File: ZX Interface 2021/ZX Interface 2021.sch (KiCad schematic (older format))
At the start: 50 parts, among them J1 AJS #1, J2 AJS #2, J3 SWAP_ROMS, J4 Cartridge, J5 JOYSTICK_EN, M1 Mounting, M2 Mounting, M3 Mounting, M4 Mounting, M5 Mounting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

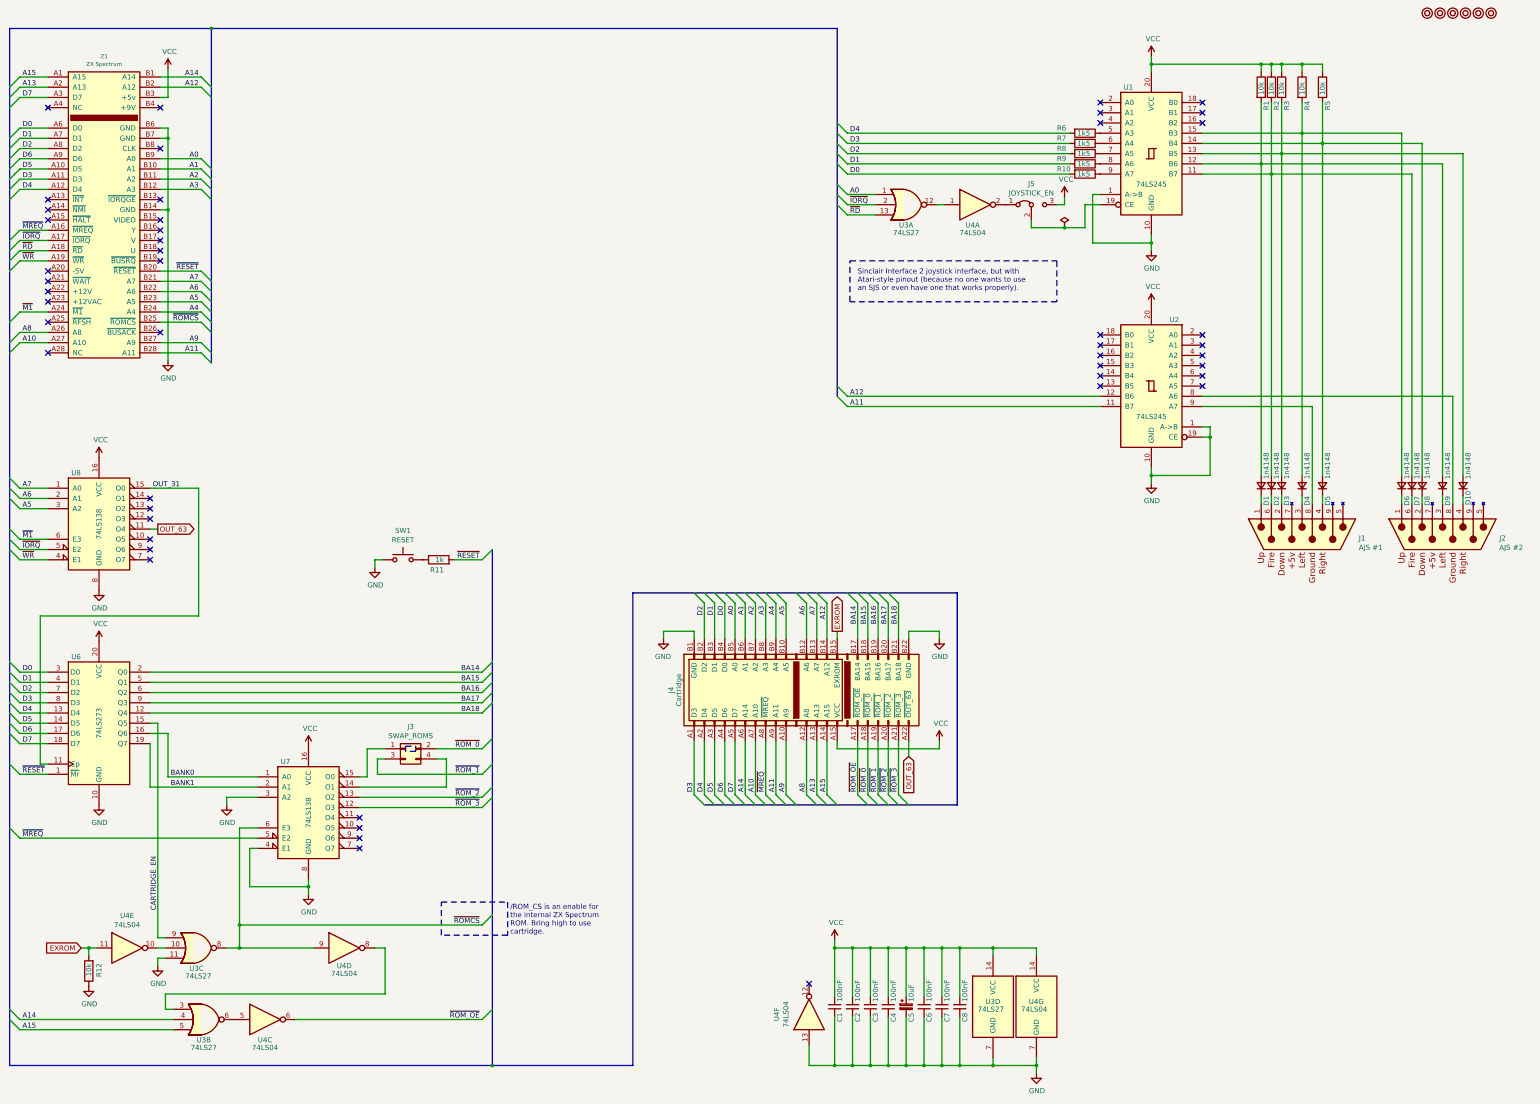
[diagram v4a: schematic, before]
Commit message: Added some artwork
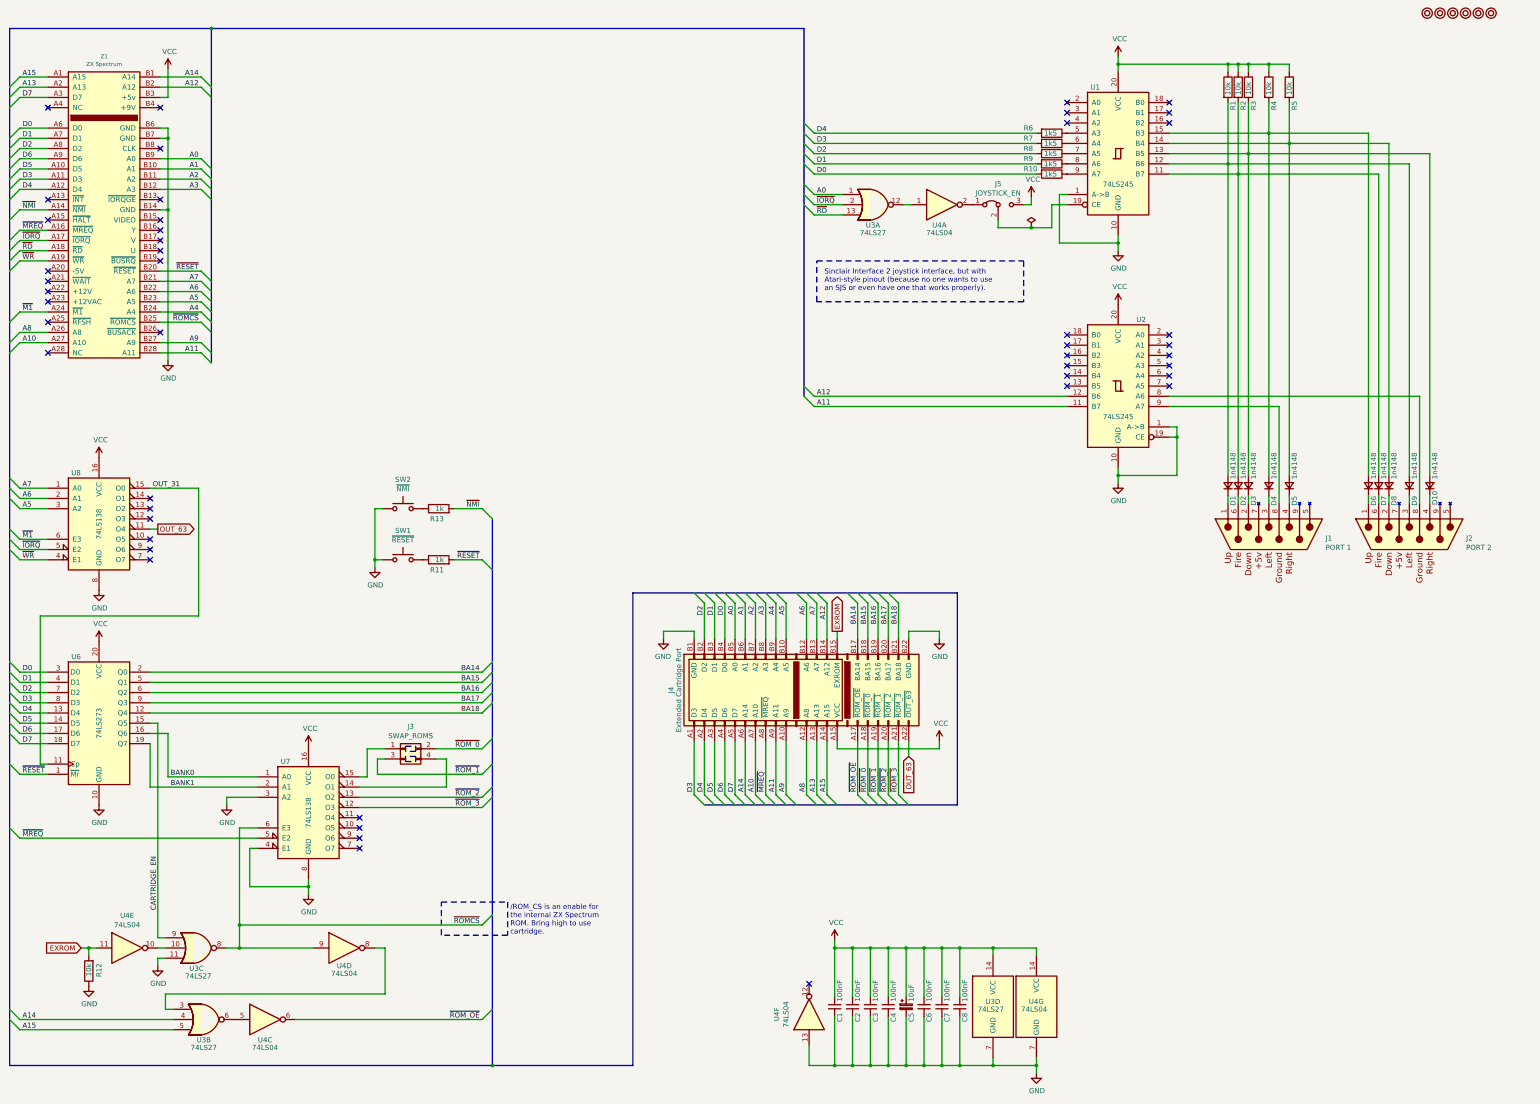
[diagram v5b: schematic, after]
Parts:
- added R13: 1k, Resistor_THT:R_Axial_DIN0207_L6.3mm_D2.5mm_P10.16mm_Horizontal, symbol Device:R
- added SW2: ~NMI, switch_cutout:SW_PUSH_6mm, symbol Switch:SW_Push
- J1: value AJS #1 -> PORT 1
- J2: value AJS #2 -> PORT 2
- J4: value Cartridge -> Extended Cartridge Port
- SW1: value RESET -> ~RESET
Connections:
- net GND: now also SW2.1
- net ~NMI: now reaches Z1.A14 (~NMI)
- net ~NMI: now also R13.2
- new net: R13.1, SW2.2
- no-connect marks 48 -> 47
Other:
- moved on the sheet: D1, D10, D2, D3, D4, D5, D6, D7, D8, D9, J1, J2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

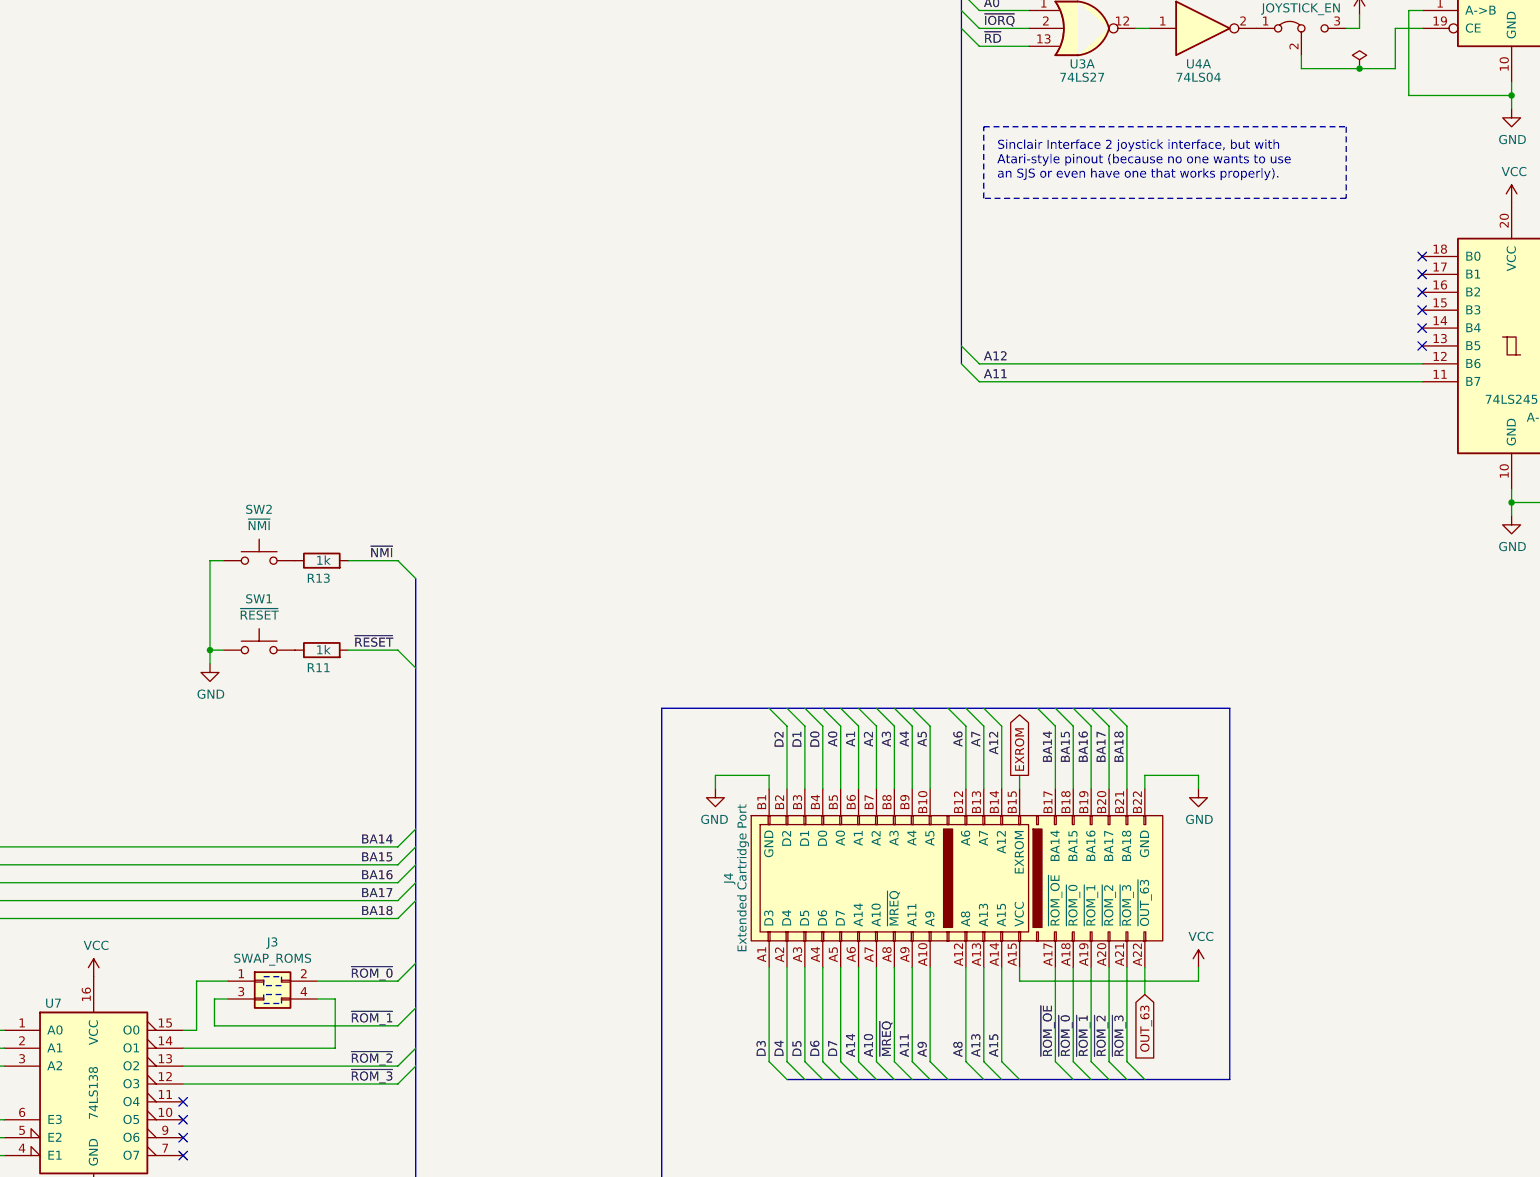
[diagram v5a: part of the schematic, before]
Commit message: Cartridge pins were mirrored, still need to change cartridges
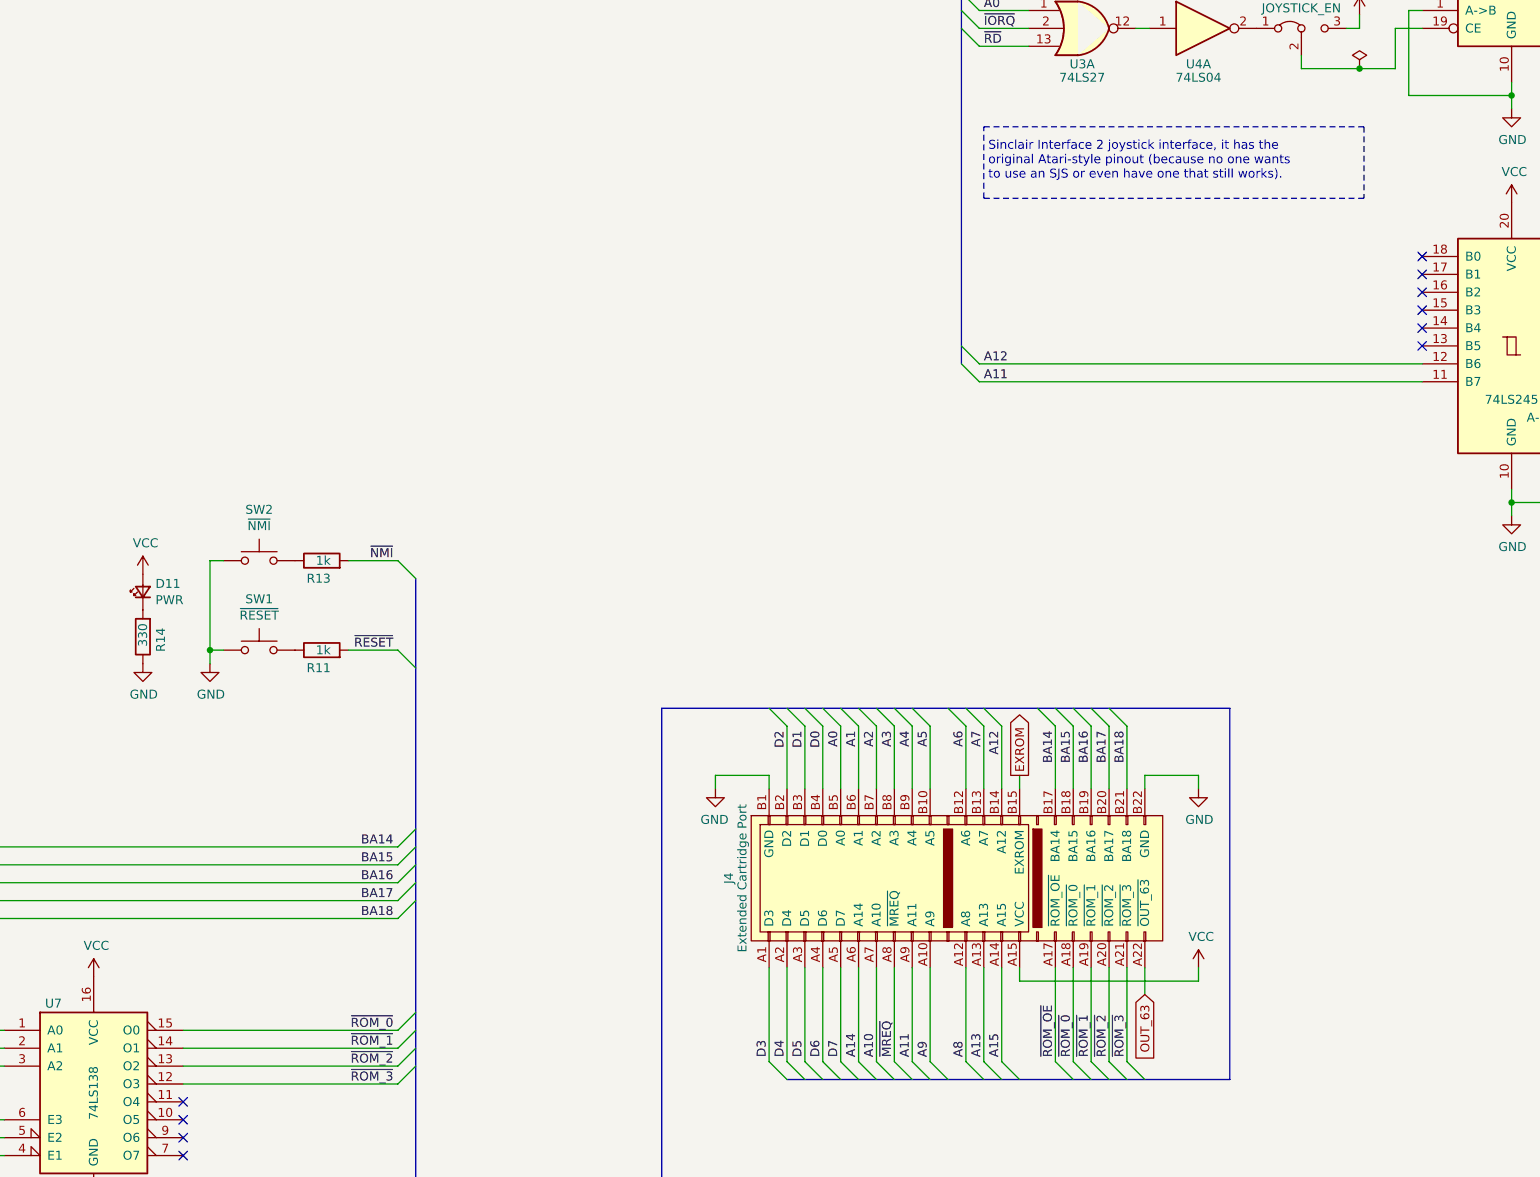
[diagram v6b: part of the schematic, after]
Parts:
- removed J3: SWAP_ROMS, Connector_PinHeader_2.54mm:PinHeader_2x02_P2.54mm_Vertical, symbol Connector_Generic:Conn_02x02_Odd_Even
- added D11: PWR, LED_THT:LED_D5.0mm, symbol Device:LED_Small
- added R14: 330, Resistor_THT:R_Axial_DIN0207_L6.3mm_D2.5mm_P10.16mm_Horizontal, symbol Device:R
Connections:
- net GND: now also R14.1
- net VCC: now also D11.2 (A)
- net ~ROM_0: now also U7.15 (O0)
- net ~ROM_1: now also U7.14 (O1)
- new net: D11.1 (K), R14.2
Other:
- note added: "Sinclair Interface 2 joystick interface, it has the \noriginal Atari-style pinout (because no one wants\nto use an SJS or even have one that still works)."
- note removed: "Sinclair Interface 2 joystick interface, but with\nAtari-style pinout (because no one wants to use\nan SJS or even have one that works properly)."
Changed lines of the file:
@@
 NoConn ~ 4900 8725
 Entry Wire Line
-	6100 8000 6200 7900
+	6100 8125 6200 8025
 NoConn ~ 9300 10050
 NoConn ~ 1850 3575
-$Comp
-L Connector_Generic:Conn_02x02_Odd_Even J3
-U 1 1 61A0CB30
-P 5350 7750
-F 0 "J3" H 5400 7967 50  0000 C CNN
-F 1 "SWAP_ROMS" H 5400 7876 50  0000 C CNN
-F 2 "Connector_PinHeader_2.54mm:PinHeader_2x02_P2.54mm_Vertical" H 5350 7750 50  0001 C CNN
-F 3 "~" H 5350 7750 50  0001 C CNN
-	1    5350 7750
-	1    0    0    -1
-$EndComp
-Entry Wire Line
-	6100 7750 6200 7650
+Entry Wire Line
+	6100 8025 6200 7925
 Entry Wire Line
 	6100 8325 6200 8225
 Entry Wire Line
 	6100 8225 6200 8125
-Text Label 6075 8000 2    50   ~ 0
+Text Label 6075 8125 2    50   ~ 0
 ~ROM_1
-Text Label 6075 7750 2    50   ~ 0
+Text Label 6075 8025 2    50   ~ 0
 ~ROM_0
 Entry Wire Line
@@
 	2850 7400 6100 7400
 Wire Wire Line
-	6100 7750 5650 7750
-Wire Notes Line
-	5450 7775 5350 7775
-Wire Notes Line
-	5450 7725 5450 7775
-Wire Notes Line
-	5350 7725 5450 7725
-Wire Notes Line
-	5350 7775 5350 7725
-Wire Wire Line
-	5750 7850 5750 8125
-Wire Wire Line
-	5650 7850 5750 7850
-Wire Wire Line
-	5075 8000 6100 8000
-Wire Wire Line
-	5075 7850 5150 7850
-Wire Wire Line
-	5075 8000 5075 7850
-Wire Wire Line
-	4975 7750 5150 7750
-Wire Wire Line
-	4975 8025 4975 7750
-Wire Wire Line
 	9300 10650 9300 10850
 Wire Wire Line
@@
 Wire Wire Line
 	2850 8125 3900 8125
-Wire Wire Line
-	4900 8025 4975 8025
-Wire Wire Line
-	4900 8125 5750 8125
 Wire Wire Line
 	4900 8225 6100 8225
@@
 Text Notes 6375 9575 0    50   ~ 0
 /ROM_CS is an enable for\nthe internal ZX Spectrum\nROM. Bring high to use\ncartridge.
-Text Notes 9450 3275 0    50   ~ 0
-Sinclair Interface 2 joystick interface, but with\nAtari-style pinout (because no one wants to use\nan SJS or even have one that works properly).
+Text Notes 9400 3275 0    50   ~ 0
+Sinclair Interface 2 joystick interface, it has the \noriginal Atari-style pinout (because no one wants\nto use an SJS or even have one that still works).
 Wire Notes Line
-	9375 2975 11400 2975
-Wire Notes Line
-	11400 2975 11400 3375
-Wire Notes Line
-	11400 3375 9375 3375
+	11500 2975 11500 3375
 Wire Notes Line
 	9375 3375 9375 2975
@@
 	11150 2650 11150 2575
 Wire Wire Line
-	11150 2650 11475 2650
-Connection ~ 11475 2650
-Wire Wire Line
-	11475 2650 11675 2650
-Wire Wire Line
 	11675 2650 11675 2425
 Wire Wire Line
 	11675 2425 11825 2425
-$Comp
-L power:PWR_FLAG #FLG0101
-U 1 1 607D1200
-P 11475 2650
-F 0 "#FLG0101" H 11475 2725 50  0001 C CNN
-F 1 "PWR_FLAG" H 11475 2823 50  0001 C CNN
-F 2 "" H 11475 2650 50  0001 C CNN
-F 3 "~" H 11475 2650 50  0001 C CNN
-	1    11475 2650
-	1    0    0    -1
-$EndComp
 Wire Bus Line
 	9250 700  3450 700
@@
 Text Label 1600 2475 0    50   ~ 0
 ~NMI
+$Comp
+L Device:R R14
+U 1 1 60553925
+P 4675 5825
+F 0 "R14" V 4575 5775 50  0000 L CNN
+F 1 "330" V 4675 5750 50  0000 L CNN
+F 2 "Resistor_THT:R_Axial_DIN0207_L6.3mm_D2.5mm_P10.16mm_Horizontal" V 4605 5825 50  0001 C CNN
+F 3 "~" H 4675 5825 50  0001 C CNN
+	1    4675 5825
+	-1   0    0    1
+$EndComp
+$Comp
+L Device:LED_Small D11
+U 1 1 6059C36A
+P 4675 5575
+F 0 "D11" V 4721 5505 50  0000 R CNN
+F 1 "PWR" V 4630 5505 50  0000 R CNN
+F 2 "LED_THT:LED_D5.0mm" V 4675 5575 50  0001 C CNN
+F 3 "~" V 4675 5575 50  0001 C CNN
+	1    4675 5575
+	0    -1   -1   0
+$EndComp
+$Comp
+L power:VCC #PWR0119
+U 1 1 6059DCD1
+P 4675 5475
+F 0 "#PWR0119" H 4675 5325 50  0001 C CNN
+F 1 "VCC" H 4690 5648 50  0000 C CNN
+F 2 "" H 4675 5475 50  0001 C CNN
+F 3 "" H 4675 5475 50  0001 C CNN
+	1    4675 5475
+	1    0    0    -1
+$EndComp
+$Comp
+L power:GND #PWR0120
+U 1 1 6059E328
+P 4675 5975
+F 0 "#PWR0120" H 4675 5725 50  0001 C CNN
+F 1 "GND" H 4680 5802 50  0000 C CNN
+F 2 "" H 4675 5975 50  0001 C CNN
+F 3 "" H 4675 5975 50  0001 C CNN
+	1    4675 5975
+	1    0    0    -1
+$EndComp
 Wire Notes Line
-	5350 7825 5350 7875
+	9375 3375 11500 3375
 Wire Notes Line
-	5350 7875 5450 7875
-Wire Notes Line
-	5450 7875 5450 7825
-Wire Notes Line
-	5450 7825 5350 7825
+	9375 2975 11500 2975
+Wire Wire Line
+	4900 8025 6100 8025
+Wire Wire Line
+	4900 8125 6100 8125
 Wire Bus Line
 	9250 700  9250 4300
@@
 Wire Bus Line
 	1475 700  1475 10850
+Wire Wire Line
+	11475 2650 11675 2650
+Wire Wire Line
+	11150 2650 11475 2650
+Connection ~ 11475 2650
+$Comp
+L power:PWR_FLAG #FLG0101
+U 1 1 607D1200
+P 11475 2650
+F 0 "#FLG0101" H 11475 2725 50  0001 C CNN
+F 1 "PWR_FLAG" H 11475 2823 50  0001 C CNN
+F 2 "" H 11475 2650 50  0001 C CNN
+F 3 "~" H 11475 2650 50  0001 C CNN
+	1    11475 2650
+	1    0    0    -1
+$EndComp
 $EndSCHEMATC
